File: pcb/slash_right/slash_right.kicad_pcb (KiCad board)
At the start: 2 copper layers, 218 x 127 mm, 138 parts, among them J1 RJ12, J2 AVR-ISP-6, J3 USB_B_Mini, SW1 SW_Push, SW10 SW_Push_45deg, SW11 SW_Push_45deg, SW12 SW_Push_45deg, SW13 SW_Push_45deg, SW14 SW_Push_45deg, SW15 SW_Push_45deg, SW16 SW_Push_45deg, SW17 SW_Push_45deg, SW18 SW_Push_45deg, SW19 SW_Push_45deg, SW2 SW_Push_45deg, SW20 SW_Push_45deg, SW21 SW_Push_45deg, SW22 SW_Push_45deg, SW23 SW_Push_45deg, SW24 SW_Push_45deg, SW25 SW_Push_45deg, SW26 SW_Push_45deg, SW27 SW_Push_45deg, SW28 SW_Push_45deg, SW29 SW_Push_45deg, SW3 SW_Push_45deg, SW30 SW_Push_45deg, SW31 SW_Push_45deg, SW32 SW_Push_45deg, SW33 SW_Push_45deg, SW34 SW_Push_45deg, SW35 SW_Push_45deg, SW36 SW_Push_45deg, SW37 SW_Push_45deg, SW38 SW_Push_45deg, SW39 SW_Push_45deg, SW4 SW_Push_45deg, SW40 SW_Push_45deg, SW41 SW_Push_45deg, SW42 SW_Push_45deg, SW43 SW_Push_45deg, SW44 SW_Push_45deg, SW45 SW_Push_45deg, SW46 SW_Push_45deg, SW47 SW_Push_45deg, SW48 SW_Push_45deg, SW49 SW_Push_45deg, SW5 SW_Push_45deg, SW50 SW_Push_45deg, SW51 SW_Push_45deg, SW52 SW_Push_45deg, SW53 SW_Push_45deg, SW54 SW_Push_45deg, SW55 SW_Push_45deg, SW56 SW_Push_45deg, SW6 SW_Push_45deg, SW7 SW_Push_45deg, SW8 SW_Push_45deg, SW9 SW_Push_45deg, U1 ATmega32U4-AU, Y1 16MHz

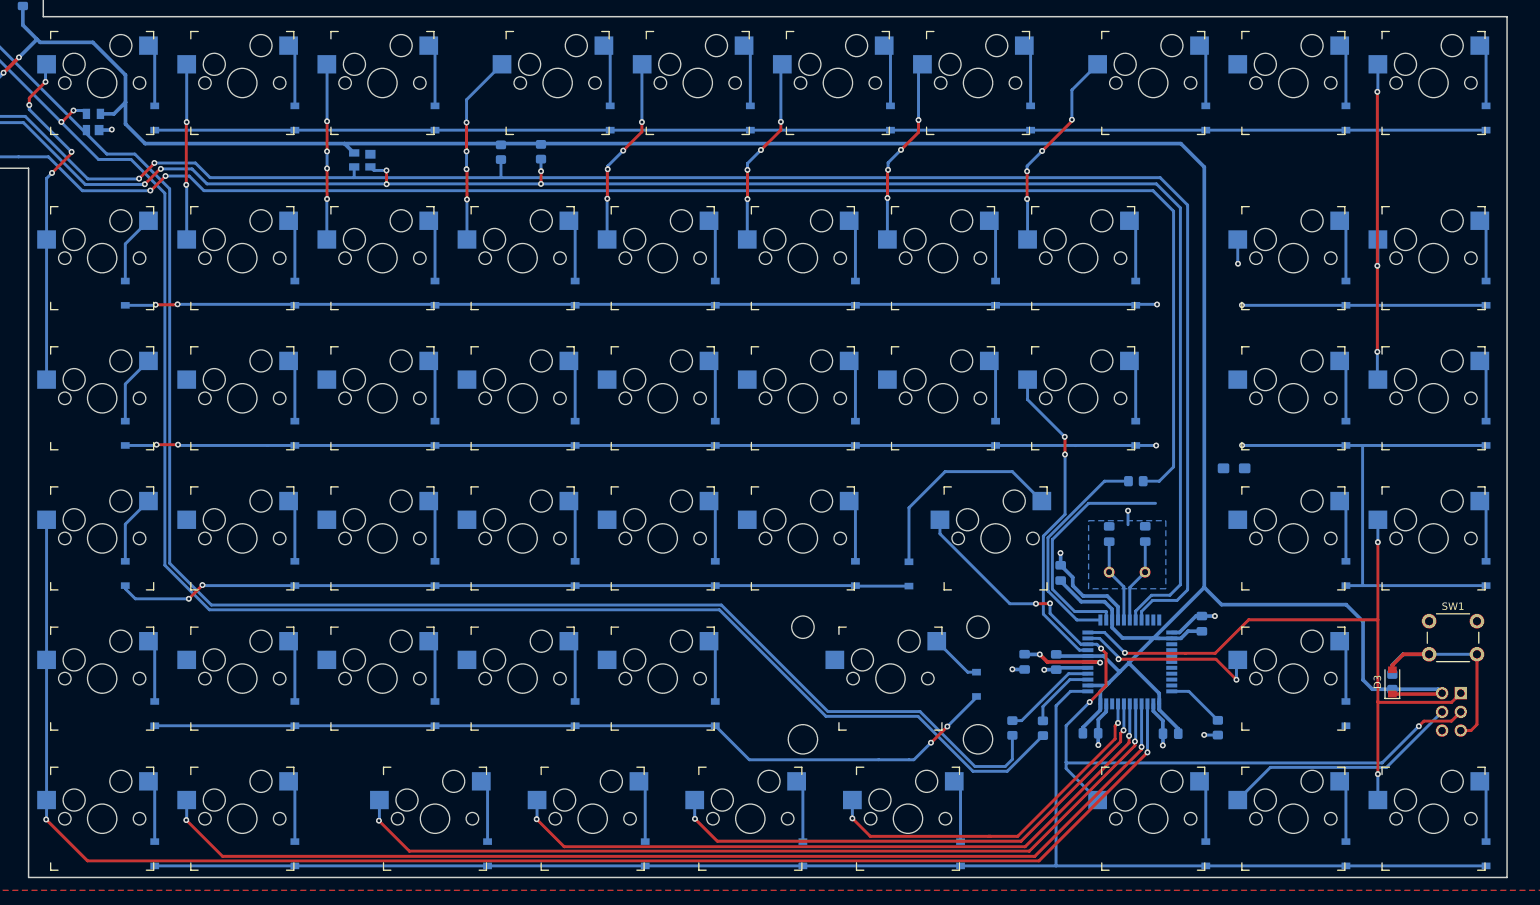
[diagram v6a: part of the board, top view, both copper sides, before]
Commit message: pcb: slash: right: Finish routing
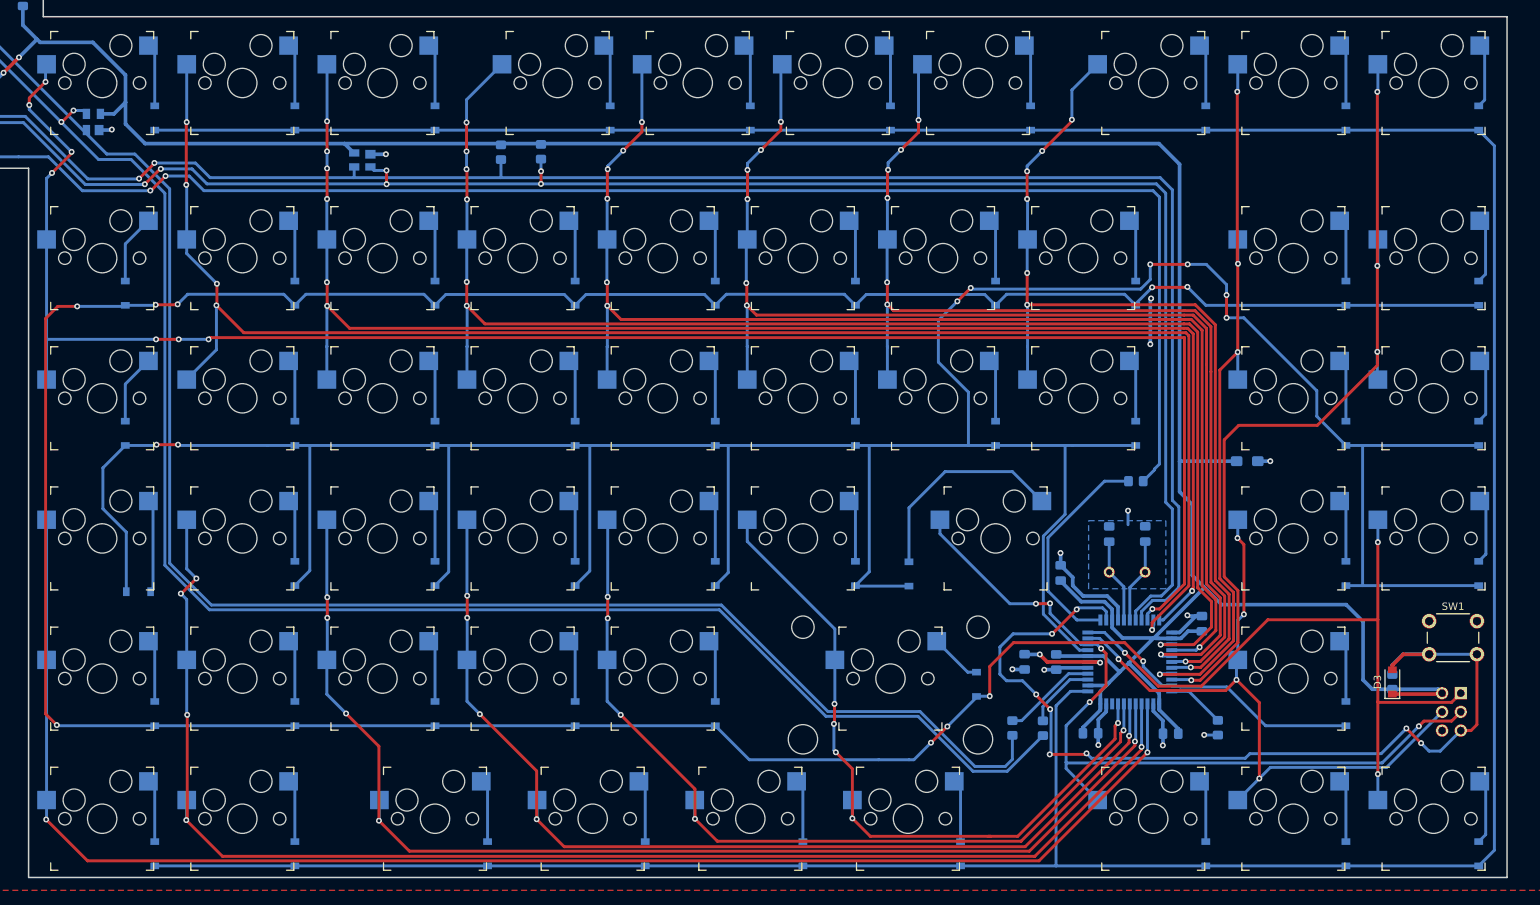
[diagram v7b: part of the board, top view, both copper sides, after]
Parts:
- moved D11 3.05 mm to (68.8, 114.4), turned to 0 degrees
- moved C1 2.03 mm to (219.6, 96.7)
- moved D55 1.00 mm to (251.0, 50.0)
- moved D56 1.00 mm to (251.0, 73.8)
- moved D57 1.00 mm to (251.0, 92.9)
- moved D58 1.00 mm to (251.0, 111.9)
- moved D59 1.00 mm to (251.0, 150.0)
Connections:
- U1 pad 20: Net-(U1-Pad20) -> /COL0
- U1 pad 21: Net-(U1-Pad21) -> /COL1
- U1 pad 22: Net-(U1-Pad22) -> /COL2
- U1 pad 25: Net-(U1-Pad25) -> /COL3
- U1 pad 26: Net-(U1-Pad26) -> /COL4
- U1 pad 27: Net-(U1-Pad27) -> /COL5
- U1 pad 28: /COL4 -> /COL6
- U1 pad 29: /COL5 -> /COL7
- U1 pad 30: /COL6 -> /COL8
- U1 pad 31: /COL8 -> /COL9
- U1 pad 32: /COL9 -> /ROW1
- U1 pad 8: /COL7 -> /ROW2
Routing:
- net /COL1: track 23.9 -> 223.7 mm, vias 2 -> 5
- net /COL0: track 47.6 -> 243.4 mm, vias 4 -> 8
- net /COL2: track 23.8 -> 203.4 mm, vias 4 -> 7
- net /COL3: track 25.8 -> 196.1 mm, vias 4 -> 7
- net /ROW1: track 290.8 -> 453.6 mm, vias 6 -> 10
- net /COL4: track 25.8 -> 175.9 mm, vias 4 -> 7
- net /COL5: track 25.8 -> 161.9 mm, vias 4 -> 7
- net /ROW2: track 319.9 -> 447.3 mm, vias 6 -> 8
- net /COL6: track 25.8 -> 141.8 mm, vias 4 -> 7
- net /ROW0: track 388.8 -> 488.6 mm
- net /COL8: track 3.31 -> 100.8 mm, vias 1 -> 4
- net /COL9: track 46.6 -> 113.0 mm, vias 3 -> 4
- net /~RST: track 64.3 -> 128.9 mm, vias 0 -> 8
- net /COL7: track 71.1 -> 126.5 mm, vias 6 -> 7
- net /COL15: track 50.0 -> 96.6 mm, vias 2 -> 5
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
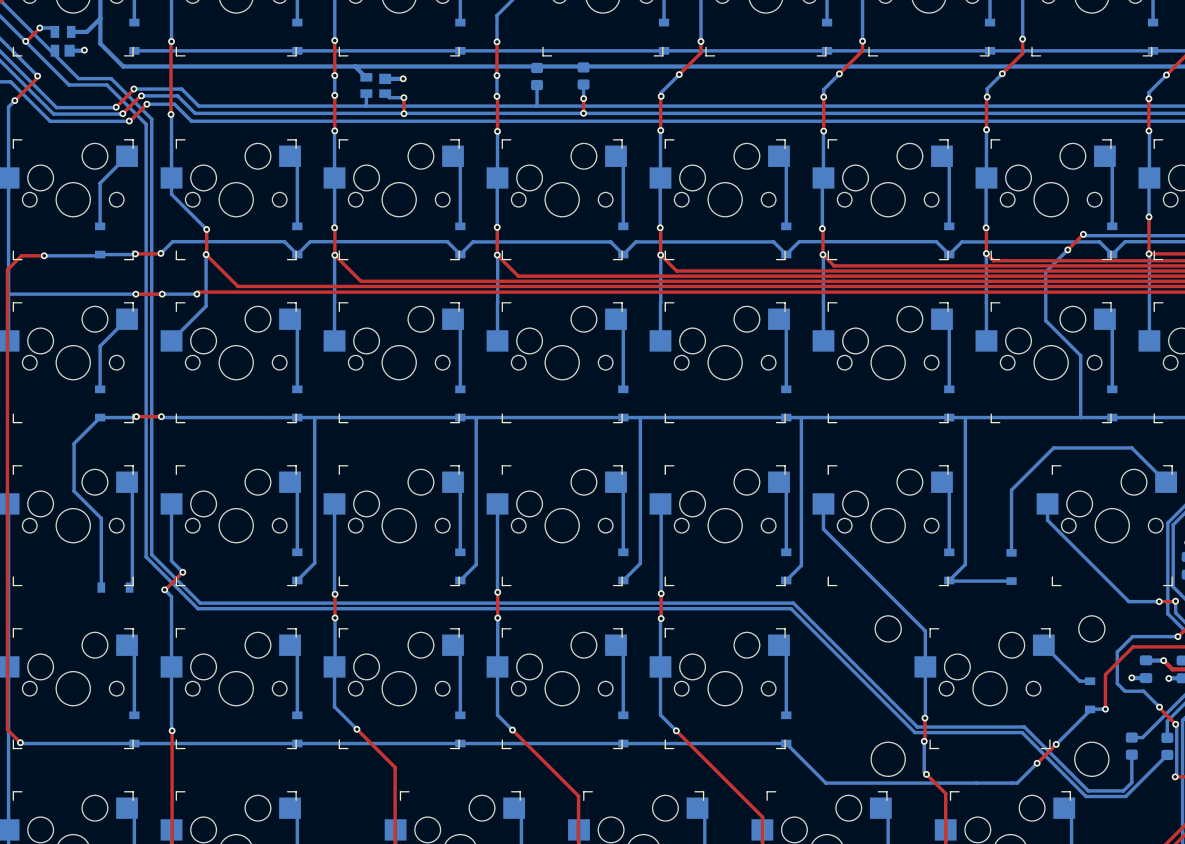
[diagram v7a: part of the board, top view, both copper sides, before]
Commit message: pcb: slash: right: Tune USB diff pair
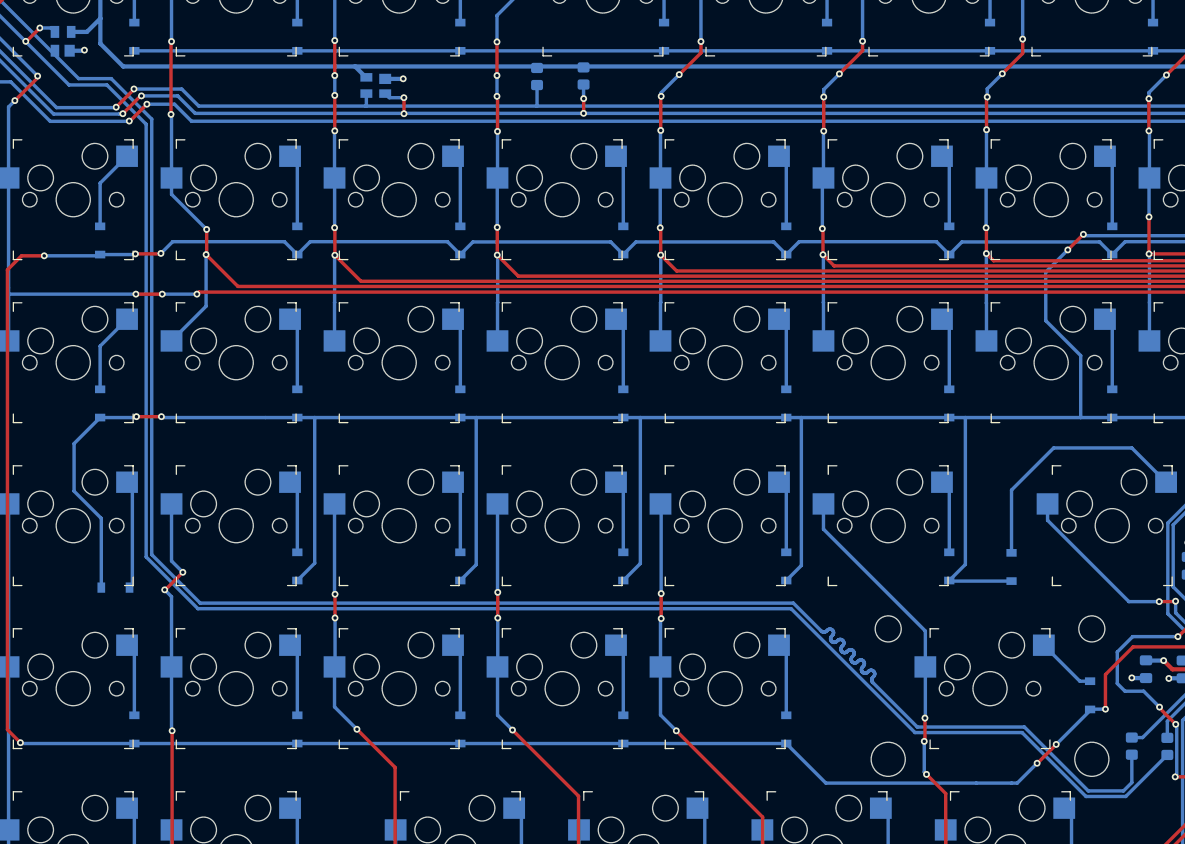
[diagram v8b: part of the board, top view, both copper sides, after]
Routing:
- net /D+: track 217.9 -> 224.2 mm
